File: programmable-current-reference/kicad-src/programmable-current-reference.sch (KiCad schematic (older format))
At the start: 26 parts, among them J1 Conn_01x02, J2 Conn_01x02, J3 Conn_01x02, J4 Conn_01x02, U1 ADR420BRZ, U2 MCP4011-103E/MS, U3 OP1177ARM, U4 OP1177ARM

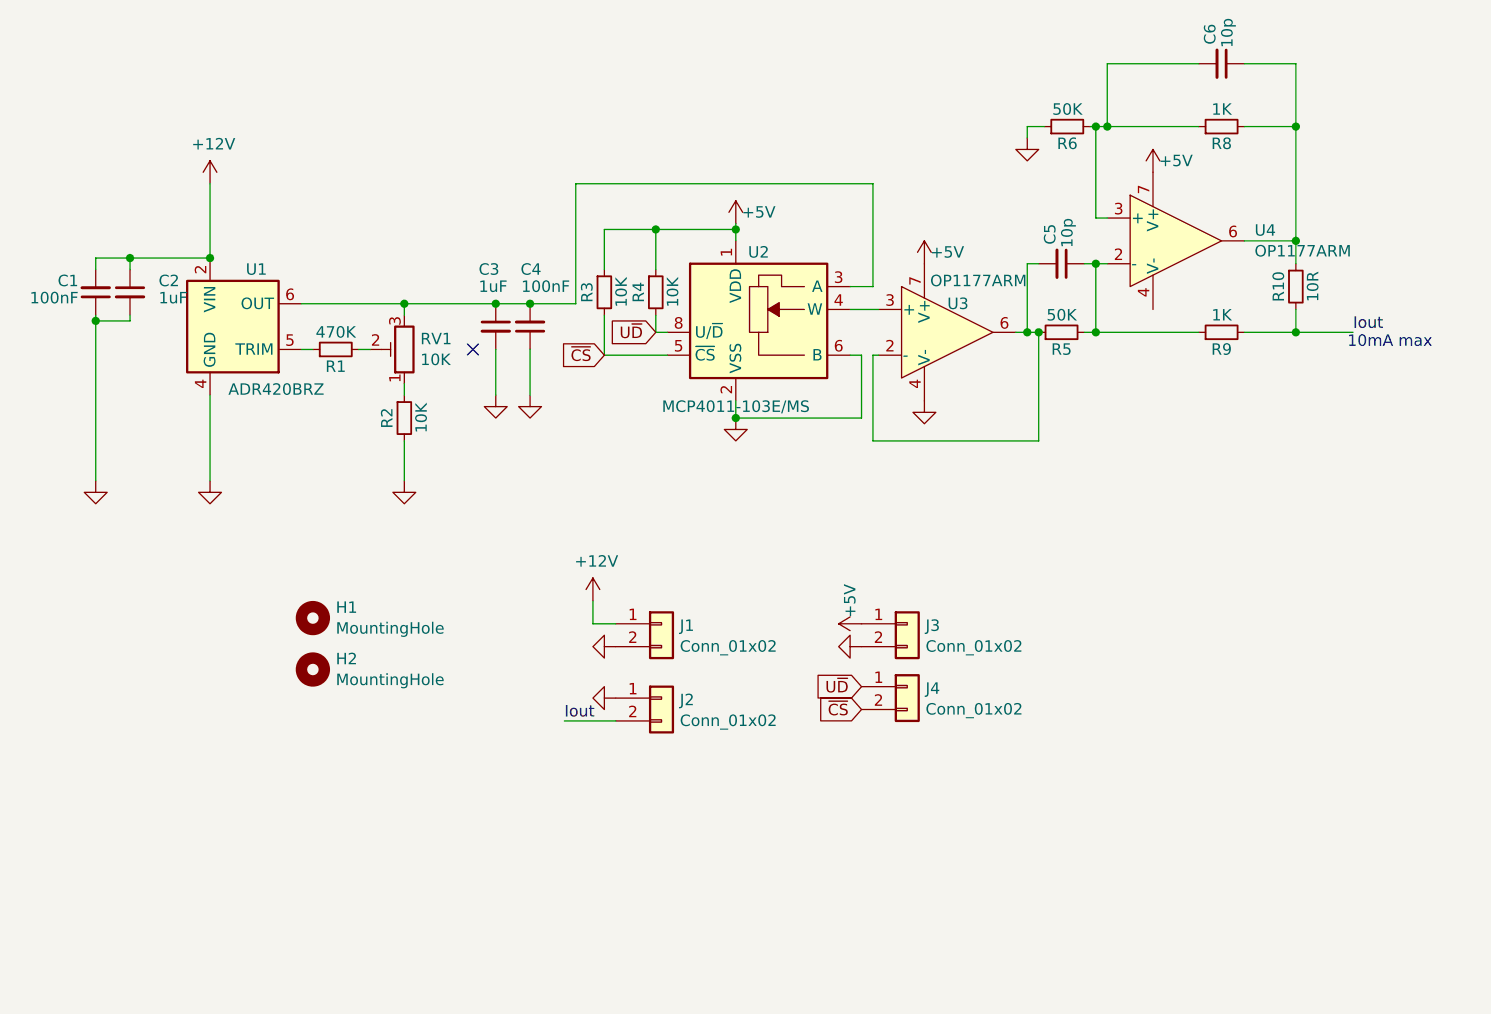
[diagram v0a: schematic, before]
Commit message: reroute portable calibrator
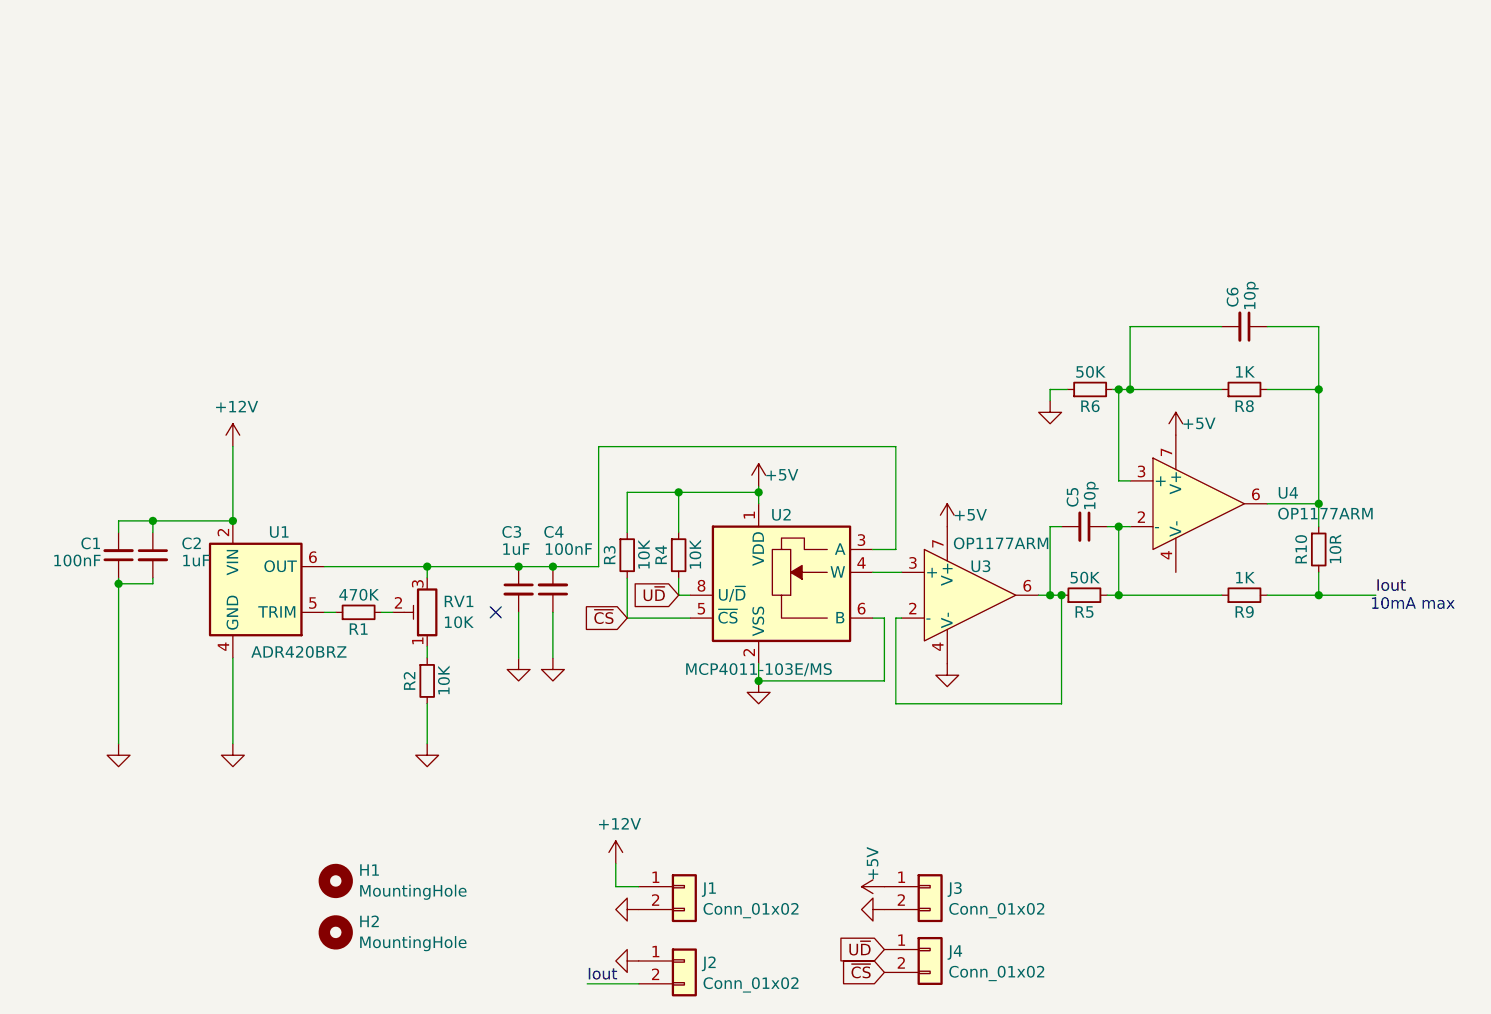
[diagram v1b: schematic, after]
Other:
- moved on the sheet: C1, C2, C3, C4, C5, C6, H1, H2, J1, J2, J3, J4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
